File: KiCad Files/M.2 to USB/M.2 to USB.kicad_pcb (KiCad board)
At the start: 4 copper layers, 22 x 26 mm, 33 parts, among them J1 M.2 A+E Key Connector, J2 Conn_2Rows-09Pins_ALT, U1 USB2422T_MJ, U2 AP2152SG-13, U3 MIC2876-5.0, U4 SN74LVC1G14DBVR, Y1 OSC24M-3.3I/S3

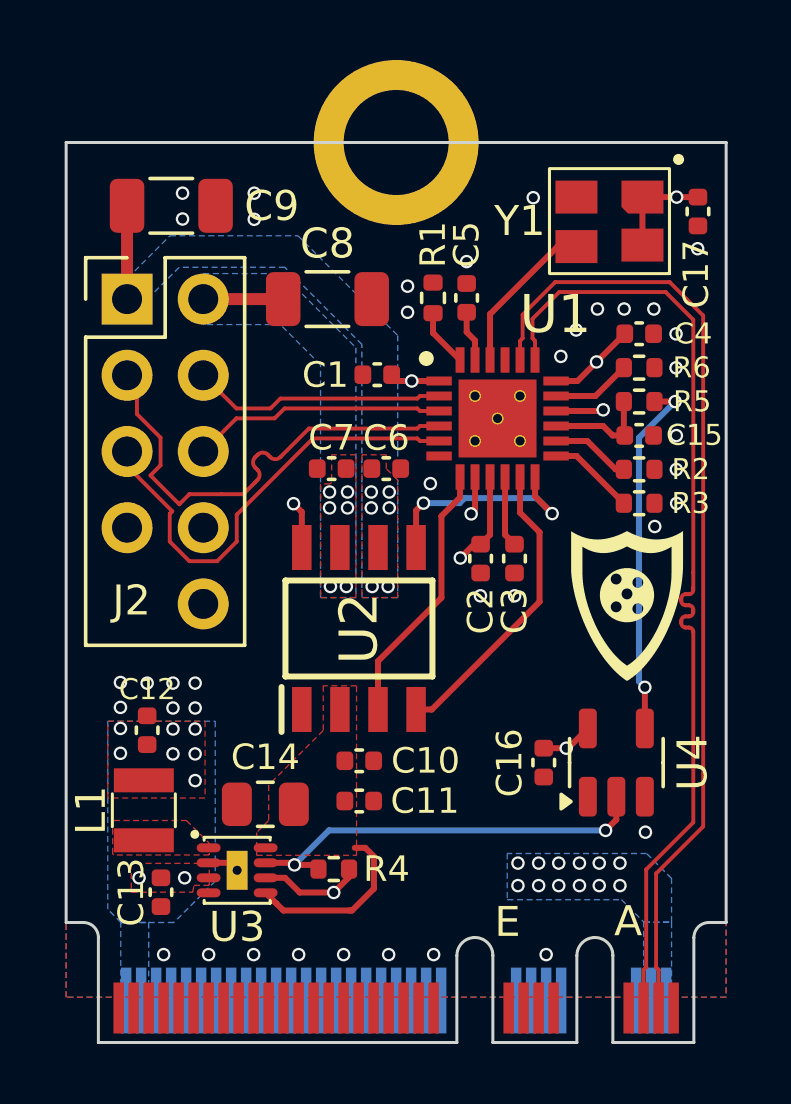
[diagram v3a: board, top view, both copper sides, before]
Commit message: optimized traces
moved the header over a bit so second usb lane could be routed in a clean fashion

made fill zones simpler

remade gerber and renders
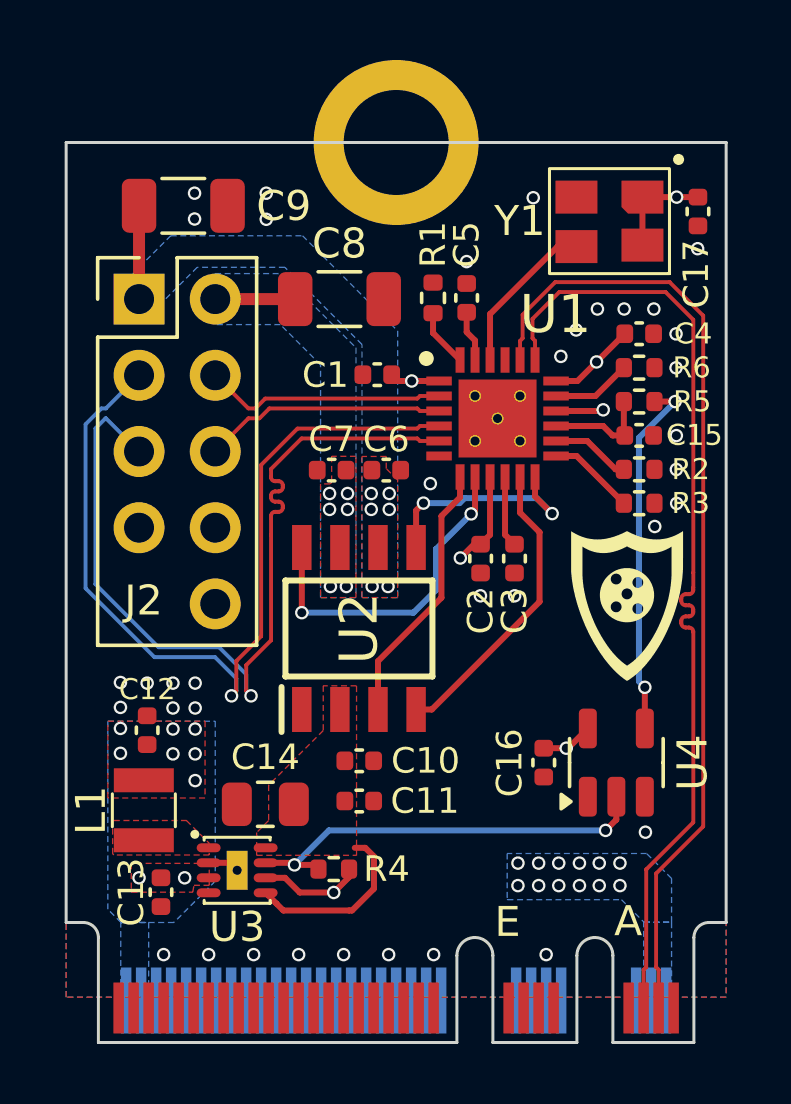
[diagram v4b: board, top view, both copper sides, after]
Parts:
- moved C8 0.40 mm to (132.1, 130.3)
- moved C9 0.40 mm to (126.9, 127.2)
- moved J2 0.40 mm to (125.4, 130.3)
- moved C6 0.05 mm to (133.7, 136.1)
- moved C7 0.05 mm to (131.8, 136.1)
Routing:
- net USBDN_D2+: track 15.7 -> 29.9 mm, vias 0 -> 1
- net USBDN_D2-: track 17.0 -> 30.6 mm, vias 0 -> 1
- net ~{FLT1}: track 9.19 -> 11.3 mm
- net GND: vias 39 -> 37

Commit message: added silkscreen version number to back
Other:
- board text added: "SuperCookie's M.2 to USB V1.1"
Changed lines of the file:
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@@
 		(layer "Edge.Cuts")
+	)
+	(gr_text "SuperCookie's M.2 to USB V1.1"
+		(at 133.96 147.79 0)
+		(layer "B.SilkS")
+		(effects
+			(font
+				(size 0.9 0.9)
+				(thickness 0.15)
+			)
+			(justify bottom mirror)
+		)
 	)
 	(segment
